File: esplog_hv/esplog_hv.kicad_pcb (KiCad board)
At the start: 2 copper layers, 16.6 x 11.8 mm, 35 parts, among them IC1 MP2359DJ-LF-Z, SW1 SW_Push, U1 ESP32-C3, U2 BMI160, Y1 Crystal_GND24

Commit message: Add component values
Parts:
- C1, C2: value C -> 10p
- C11, C13, C14: value C -> 4.7u
- C12, C3, C4, C6, C8, C9: value C -> 100n
- C7: value C -> 22u
- D1: value D -> -
- IC1: value MP2359DJ-LF-Z -> RY8310
- L2: value L -> VLS3012HBX-4R7M
- R1, R3, R4: value R -> 10k
- R2: value R -> 31.6k
- Y1: value Crystal_GND24 -> 40M

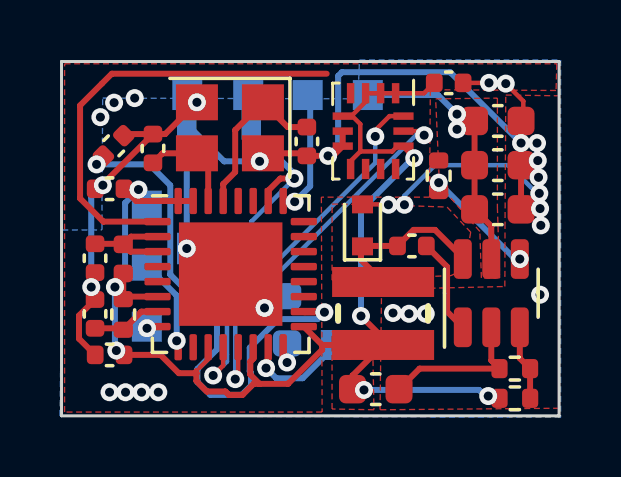
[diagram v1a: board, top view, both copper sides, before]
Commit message: esplog_hv: change the capacitor value on chip_en to 1u
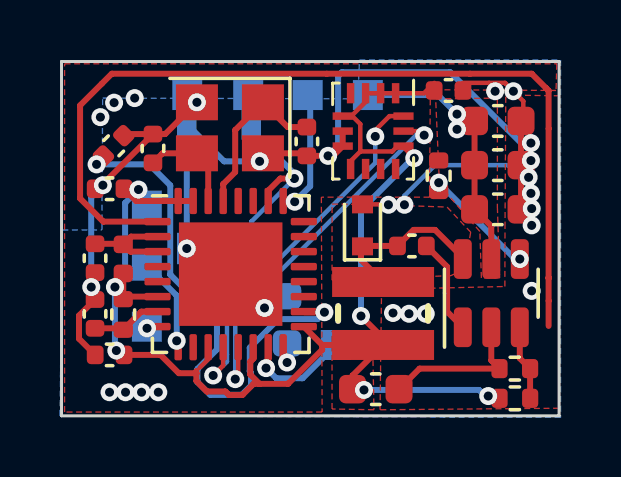
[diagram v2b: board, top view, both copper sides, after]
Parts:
- C3: value 100n -> 1u
- moved C12 0.25 mm to (95.6, 54.6)
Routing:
- net /ANT: track 14.7 -> 30.1 mm
- net GND: track 56.8 -> 54.0 mm, vias 29 -> 28

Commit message: add gerbers for esplog-hv
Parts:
- L1: value L -> 2n
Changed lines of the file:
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@@
       (effects (font (size 1 1) (thickness 0.15)))
     )
-    (fp_text value "L" (at 0 1.17 90) (layer "F.Fab") hide
+    (fp_text value "2n" (at 0 1.17 90) (layer "F.Fab") hide
       (effects (font (size 1 1) (thickness 0.15)))
     )
@@
     (property "Sheetfile" "File: esplog_hv.kicad_sch")
     (property "Sheetname" "")
-    (attr exclude_from_pos_files)
+    (attr exclude_from_pos_files exclude_from_bom)
     (fp_text reference "TP7" (at 0 1.448) (layer "B.SilkS") hide
       (effects (font (size 1 1) (thickness 0.15)) (justify mirror))
@@
     (property "Sheetfile" "File: esplog_hv.kicad_sch")
     (property "Sheetname" "")
-    (attr exclude_from_pos_files)
+    (attr exclude_from_pos_files exclude_from_bom)
     (fp_text reference "TP4" (at 0 1.448) (layer "B.SilkS") hide
       (effects (font (size 1 1) (thickness 0.15)) (justify mirror))
@@
     (property "Sheetfile" "File: esplog_hv.kicad_sch")
     (property "Sheetname" "")
-    (attr exclude_from_pos_files)
+    (attr exclude_from_pos_files exclude_from_bom)
     (fp_text reference "TP5" (at 0 1.448) (layer "B.SilkS") hide
       (effects (font (size 1 1) (thickness 0.15)) (justify mirror))
@@
     (property "Sheetfile" "File: esplog_hv.kicad_sch")
     (property "Sheetname" "")
-    (attr exclude_from_pos_files)
+    (attr exclude_from_pos_files exclude_from_bom)
     (fp_text reference "TP2" (at 0 1.448) (layer "B.SilkS") hide
       (effects (font (size 1 1) (thickness 0.15)) (justify mirror))
@@
     (property "Sheetfile" "File: esplog_hv.kicad_sch")
     (property "Sheetname" "")
-    (attr exclude_from_pos_files)
+    (attr exclude_from_pos_files exclude_from_bom)
     (fp_text reference "TP1" (at 0 1.448) (layer "B.SilkS") hide
       (effects (font (size 1 1) (thickness 0.15)) (justify mirror))
@@
     (property "Sheetfile" "File: esplog_hv.kicad_sch")
     (property "Sheetname" "")
-    (attr exclude_from_pos_files)
+    (attr exclude_from_pos_files exclude_from_bom)
     (fp_text reference "TP3" (at 0 1.448) (layer "B.SilkS") hide
       (effects (font (size 1 1) (thickness 0.15)) (justify mirror))
@@
     (property "Sheetfile" "File: esplog_hv.kicad_sch")
     (property "Sheetname" "")
-    (attr exclude_from_pos_files)
+    (attr exclude_from_pos_files exclude_from_bom)
     (fp_text reference "TP6" (at 0 1.448) (layer "B.SilkS") hide
       (effects (font (size 1 1) (thickness 0.15)) (justify mirror))
@@
     (property "Sheetfile" "File: esplog_hv.kicad_sch")
     (property "Sheetname" "")
-    (attr exclude_from_pos_files)
+    (attr exclude_from_pos_files exclude_from_bom)
     (fp_text reference "TP8" (at 0 1.448) (layer "B.SilkS") hide
       (effects (font (size 1 1) (thickness 0.15)) (justify mirror))
